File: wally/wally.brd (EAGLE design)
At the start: 41 x 101 mm, 94 parts, among them IC1 ESP32-S3-WROOM-1U-N16, IC2 XTLV61048DBVR, IC3 TLV1117LV33DCYR, IC4 DPS310XTSA1, IC5 BMI323, IC6 MCP96L00T-E_MX, IC7 MLX90395KLW-BBA-001-SP, J1 MSD-4-A, J2 QWIIC_RIGHT_ANGLE, J3 QWIIC_RIGHT_ANGLE, J4 S2B-PH-K-S(LF)(SN), J6 USBC, U1 RA-01H

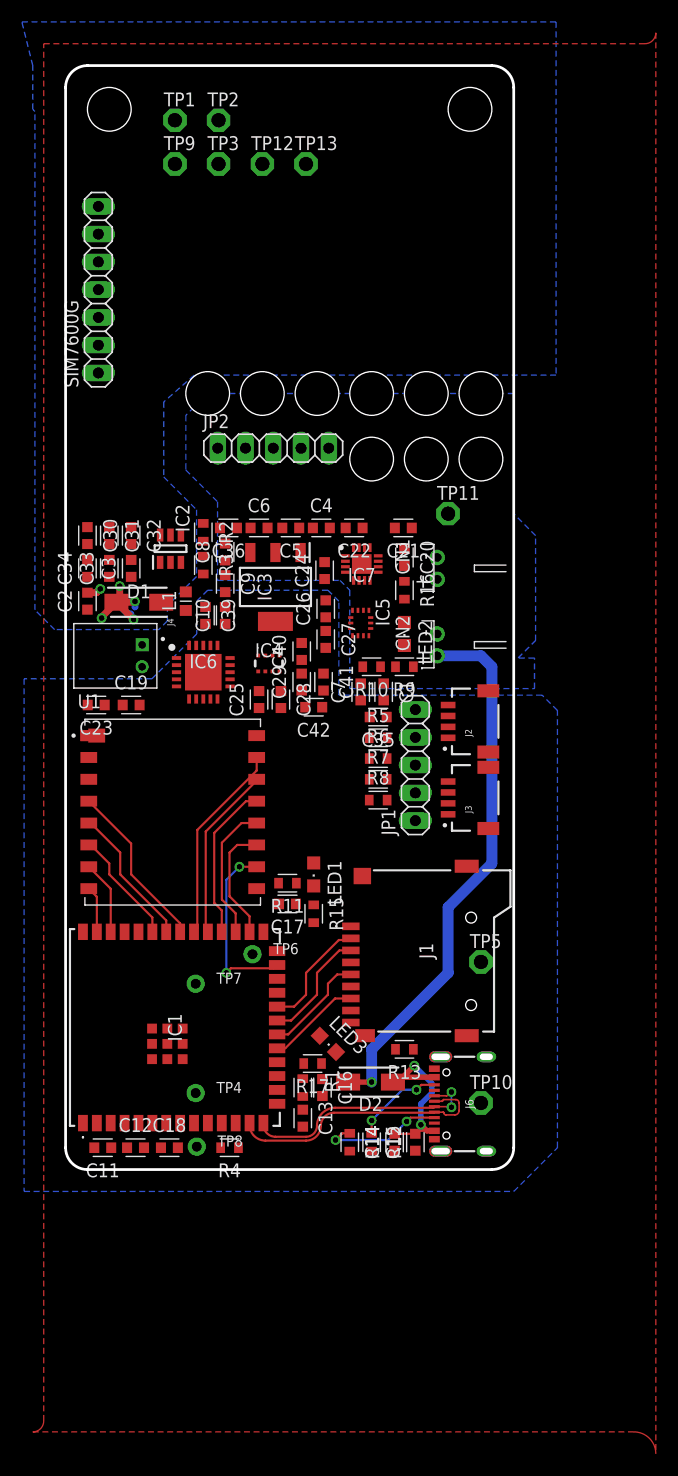
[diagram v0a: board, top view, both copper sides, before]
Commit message: high current traces
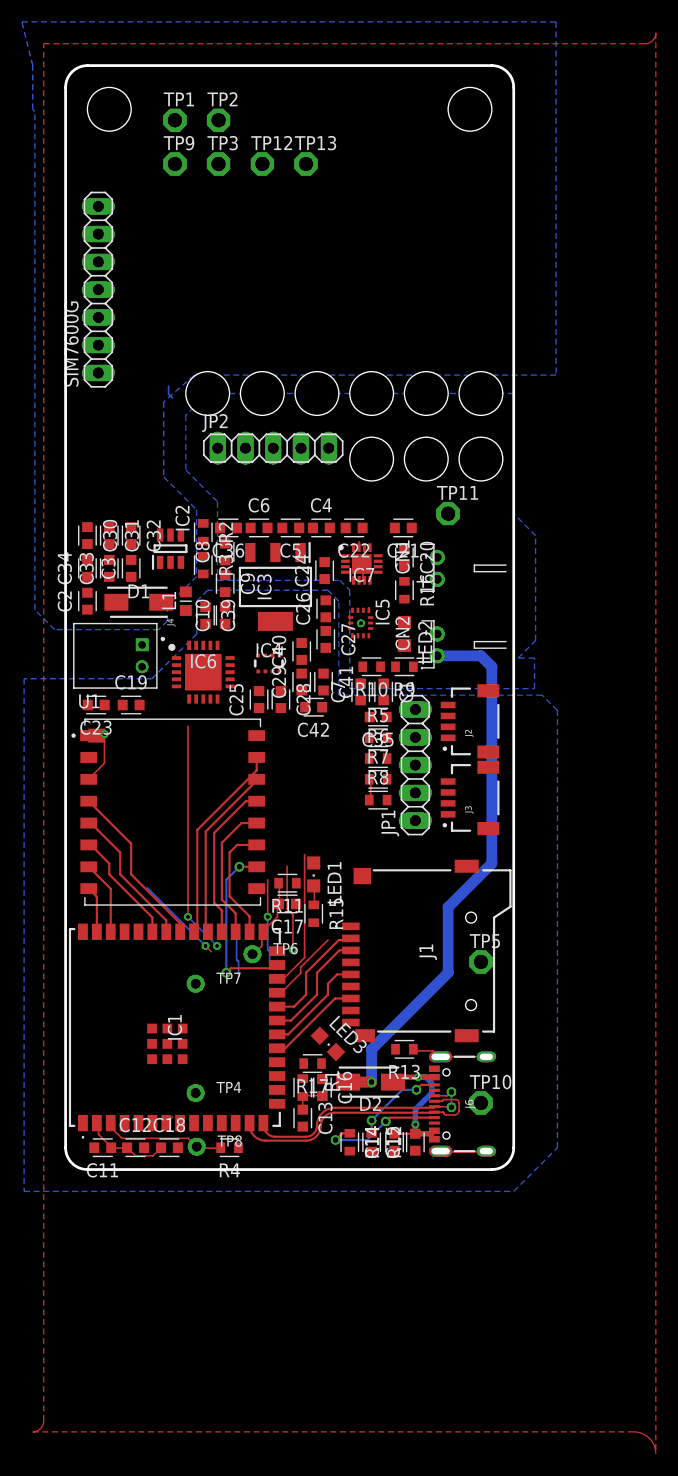
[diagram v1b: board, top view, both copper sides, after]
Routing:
- net RX1: track 0.00 -> 21.5 mm, vias 0 -> 2
- net 3V3: track 0.00 -> 18.3 mm, vias 0 -> 1
- net EN: track 0.00 -> 14.6 mm
- net SDA0: track 0.96 -> 14.0 mm
- net N$21: track 0.00 -> 11.3 mm
- net VSIM: track 10.9 -> 0.00 mm, vias 5 -> 0
- net SCL1: track 0.00 -> 9.54 mm, vias 0 -> 1
- net VSENSE: track 0.00 -> 9.32 mm, vias 0 -> 1
- net PPS: track 0.00 -> 8.41 mm, vias 0 -> 1
- net SCL0: track 0.00 -> 7.85 mm, vias 0 -> 1
- net BOOT: track 0.00 -> 7.64 mm
- net SDA1: track 0.00 -> 5.20 mm
- net VBUS: track 17.9 -> 15.8 mm
- net N$1: track 0.00 -> 1.76 mm
- net GND: track 0.00 -> 1.73 mm
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
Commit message: apply jlc drc
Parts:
- moved JP2 6.38 mm to (24.0, -31.0)
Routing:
- net VCC: track 51.6 -> 49.4 mm
- net TX1: track 1.44 -> 0.23 mm

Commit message: spider vsim
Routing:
- net VSIM: track 0.00 -> 21.4 mm, vias 0 -> 7
- net RX1: track 21.5 -> 0.30 mm, vias 2 -> 0
- net PPS: track 8.41 -> 0.11 mm, vias 1 -> 0
- net VSENSE: track 9.32 -> 1.60 mm, vias 1 -> 0
- net 3V3: track 18.3 -> 13.6 mm, vias 1 -> 0
- net SDA1: track 5.20 -> 0.68 mm
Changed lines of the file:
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@@
 <wire x1="27.9146" y1="-65.2526" x2="27.7848" y2="-65.3" width="0.1524" layer="1"/>
 <wire x1="27.9146" y1="-63.4746" x2="27.7848" y2="-63.4" width="0.1524" layer="1"/>
-<wire x1="3.556" y1="-63.8302" x2="3.556" y2="-61.1632" width="0.1524" layer="1"/>
-<wire x1="2.1336" y1="-65.2526" x2="3.556" y2="-63.8302" width="0.1524" layer="1"/>
 <wire x1="2.1336" y1="-65.2526" x2="2.1179" y2="-65.3" width="0.1524" layer="1"/>
 <wire x1="5.5118" y1="-99.0346" x2="4.2672" y2="-99.0346" width="0.1524" layer="1"/>
@@
 <wire x1="2.8448" y1="-96.7232" x2="2.86" y2="-96.75" width="0.1524" layer="1"/>
 <wire x1="29.5148" y1="-59.563" x2="29.3746" y2="-59.6" width="0.1524" layer="1"/>
-<via x="3.556" y="-61.1632" extent="1-16" drill="0.35"/>
 <wire x1="21.7" y1="-92.6848" x2="8.7254" y2="-99" width="0" layer="19" extent="1-1"/>
 <wire x1="25.9588" y1="-82.1436" x2="21.8694" y2="-92.6338" width="0" layer="19" extent="1-1"/>
@@
 <wire x1="27.9146" y1="-63.2968" x2="27.9146" y2="-61.5188" width="0" layer="19" extent="1-1"/>
 <wire x1="27.9146" y1="-65.2526" x2="27.9146" y2="-63.4746" width="0" layer="19" extent="1-1"/>
-<wire x1="3.5746" y1="-58.5" x2="3.556" y2="-61.1632" width="0" layer="19" extent="1-1"/>
-<wire x1="5.2254" y1="-58.5" x2="3.5746" y2="-58.5" width="0" layer="19" extent="1-1"/>
 <wire x1="34.4932" y1="-60.6298" x2="32" y2="-58.92" width="0" layer="19" extent="1-1"/>
 <wire x1="23.6" y1="-57.1746" x2="27.7368" y2="-61.341" width="0" layer="19" extent="1-1"/>
@@
 <wire x1="12.6" y1="-57.95" x2="17.7" y2="-57.2254" width="0" layer="19" extent="1-1"/>
 <wire x1="34.8488" y1="-67.3862" x2="34.4932" y2="-60.6298" width="0" layer="19" extent="1-1"/>
+<wire x1="5.2254" y1="-58.5" x2="12.6" y2="-57.95" width="0" layer="19" extent="1-1"/>
+<wire x1="3.5746" y1="-58.5" x2="5.2254" y2="-58.5" width="0" layer="19" extent="1-1"/>
+<wire x1="2.1336" y1="-65.2526" x2="3.5746" y2="-58.5" width="0" layer="19" extent="1-1"/>
 <wire x1="18" y1="-9" x2="19.2" y2="-44.55" width="0" layer="19" extent="1-1"/>
 </signal>
@@
 <vertex x="-3" y="0"/>
 </polygon>
-<wire x1="2" y1="-48.2254" x2="4.65" y2="-49.1" width="0" layer="19" extent="1-1"/>
-<wire x1="2" y1="-45.2254" x2="2" y2="-48.2254" width="0" layer="19" extent="1-1"/>
-<wire x1="2" y1="-43.7746" x2="2" y2="-45.2254" width="0" layer="19" extent="1-1"/>
-<wire x1="4" y1="-43.7746" x2="2" y2="-43.7746" width="0" layer="19" extent="1-1"/>
+<wire x1="2" y1="-43.7746" x2="6" y2="-43.7746" width="0.2" layer="1"/>
+<wire x1="2" y1="-45.2254" x2="4" y2="-45.2254" width="0.2" layer="1"/>
+<wire x1="2" y1="-45.2254" x2="2" y2="-43.7746" width="0.2" layer="1"/>
+<wire x1="2" y1="-48.2254" x2="2.8966" y2="-49.122" width="0.2" layer="1"/>
+<wire x1="2.8966" y1="-49.122" x2="3.175" y2="-49.122" width="0.2" layer="1"/>
+<wire x1="4.327" y1="-49.1" x2="3.144" y2="-47.917" width="0.5" layer="1"/>
+<wire x1="3.144" y1="-47.891" x2="3.144" y2="-47.917" width="0.2" layer="1"/>
+<wire x1="4.65" y1="-49.1" x2="4.327" y2="-49.1" width="0.2" layer="1"/>
+<via x="3.144" y="-47.891" extent="1-16" drill="0.35"/>
+<wire x1="4.65" y1="-49.1" x2="4.728" y2="-49.022" width="0.2" layer="1"/>
+<wire x1="4.728" y1="-49.022" x2="6.223" y2="-49.022" width="0.5" layer="1"/>
+<via x="6.223" y="-49.022" extent="1-16" drill="0.35"/>
+<wire x1="6.014" y1="-50.152" x2="4.962" y2="-49.1" width="0.5" layer="1"/>
+<wire x1="4.65" y1="-49.1" x2="4.962" y2="-49.1" width="0.2" layer="1"/>
+<wire x1="6.123" y1="-50.152" x2="6.161" y2="-50.114" width="0.2" layer="1"/>
+<wire x1="6.123" y1="-50.152" x2="6.014" y2="-50.152" width="0.2" layer="1"/>
+<via x="6.161" y="-50.114" extent="1-16" drill="0.35"/>
+<wire x1="4.65" y1="-49.1" x2="4.99" y2="-49.1" width="0.2" layer="1"/>
+<wire x1="6.161" y1="-47.891" x2="6.161" y2="-47.929" width="0.2" layer="1"/>
+<wire x1="6.161" y1="-47.929" x2="4.99" y2="-49.1" width="0.5" layer="1"/>
+<via x="6.161" y="-47.891" extent="1-16" drill="0.35"/>
+<wire x1="4.65" y1="-49.1" x2="4.65" y2="-50.191" width="0.5" layer="1"/>
+<wire x1="4.65" y1="-50.191" x2="4.716" y2="-50.257" width="0.2" layer="1"/>
+<via x="4.716" y="-50.257" extent="1-16" drill="0.35"/>
+<wire x1="4.65" y1="-49.1" x2="4.498" y2="-49.1" width="0.2" layer="1"/>
+<wire x1="4.498" y1="-49.1" x2="3.2505" y2="-50.3475" width="0.5" layer="1"/>
+<wire x1="3.2505" y1="-50.3475" x2="3.144" y2="-50.241" width="0.2" layer="1"/>
+<via x="3.144" y="-50.241" extent="1-16" drill="0.35"/>
+<wire x1="4.65" y1="-49.1" x2="4.628" y2="-49.122" width="0.2" layer="1"/>
+<wire x1="4.628" y1="-49.122" x2="3.175" y2="-49.122" width="0.5" layer="1"/>
+<via x="3.175" y="-49.122" extent="1-16" drill="0.35"/>
 <wire x1="4" y1="-45.2254" x2="4" y2="-43.7746" width="0" layer="19" extent="1-1"/>
-<wire x1="6" y1="-43.7746" x2="4" y2="-43.7746" width="0" layer="19" extent="1-1"/>
+<wire x1="3.144" y1="-47.891" x2="4" y2="-45.2254" width="0" layer="19" extent="1-1"/>
 <wire x1="12.6" y1="-41.8848" x2="6" y2="-43.7746" width="0" layer="19" extent="1-1"/>
 <wire x1="14.1254" y1="-42.3" x2="12.6" y2="-41.8848" width="0" layer="19" extent="1-1"/>
-<wire x1="3" y1="-17.96" x2="12.6" y2="-41.8848" width="0" layer="19" extent="1-1"/>
 </signal>
 <signal name="SLEEP">
@@
 <wire x1="34.8488" y1="-66.675" x2="35" y2="-66.5" width="0.1524" layer="1"/>
 <wire x1="6.7564" y1="-96.3676" x2="6.7564" y2="-96.7232" width="0.1524" layer="1"/>
-<wire x1="15.8242" y1="-81.9658" x2="15.8242" y2="-83.3882" width="0.1524" layer="16"/>
-<wire x1="15.6464" y1="-81.788" x2="15.8242" y2="-81.9658" width="0.1524" layer="16"/>
-<wire x1="15.6464" y1="-78.9432" x2="15.6464" y2="-81.788" width="0.1524" layer="16"/>
 <wire x1="6.7564" y1="-96.7232" x2="6.67" y2="-96.75" width="0.1524" layer="1"/>
-<wire x1="15.8242" y1="-83.3882" x2="6.7564" y2="-96.3676" width="0" layer="19" extent="1-16"/>
-<wire x1="29.4152" y1="-65.3" x2="15.6464" y2="-78.9432" width="0" layer="19" extent="1-16"/>
+<wire x1="29.4152" y1="-65.3" x2="6.7564" y2="-96.3676" width="0" layer="19" extent="1-1"/>
 <wire x1="34.8488" y1="-66.675" x2="29.4152" y2="-65.3" width="0" layer="19" extent="1-1"/>
 </signal>
@@
 <wire x1="30.0482" y1="-54.9402" x2="30.1848" y2="-55" width="0.1524" layer="1"/>
 <wire x1="28.448" y1="-55.118" x2="28.8036" y2="-55.118" width="0.1524" layer="1"/>
-<wire x1="18.4912" y1="-77.8764" x2="18.4912" y2="-74.4982" width="0.1524" layer="1"/>
-<wire x1="18.4912" y1="-80.899" x2="18.4912" y2="-77.8764" width="0.1524" layer="16"/>
-<wire x1="18.669" y1="-81.0768" x2="18.4912" y2="-80.899" width="0.1524" layer="16"/>
-<wire x1="18.669" y1="-82.1436" x2="18.669" y2="-81.0768" width="0.1524" layer="16"/>
 <wire x1="9.2456" y1="-96.7232" x2="9.779" y2="-96.1898" width="0.1524" layer="1"/>
 <wire x1="28.8036" y1="-55.118" x2="28.8152" y2="-55" width="0.1524" layer="1"/>
 <wire x1="9.2456" y1="-96.7232" x2="9.21" y2="-96.75" width="0.1524" layer="1"/>
-<via x="18.4912" y="-77.8764" extent="1-16" drill="0.35"/>
-<wire x1="18.669" y1="-82.1436" x2="9.779" y2="-96.1898" width="0" layer="19" extent="1-16"/>
-<wire x1="28.448" y1="-55.118" x2="18.4912" y2="-74.4982" width="0" layer="19" extent="1-1"/>
+<wire x1="28.448" y1="-55.118" x2="9.779" y2="-96.1898" width="0" layer="19" extent="1-1"/>
 <wire x1="30.0482" y1="-54.9402" x2="28.9814" y2="-54.9402" width="0" layer="19" extent="1-1"/>
 </signal>
@@
 <contactref element="JP2" pad="3"/>
 <contactref element="IC1" pad="10"/>
-<wire x1="11.2014" y1="-77.8764" x2="13.8684" y2="-80.5434" width="0.1524" layer="16"/>
-<wire x1="11.2014" y1="-60.452" x2="11.2014" y2="-77.8764" width="0.1524" layer="1"/>
 <wire x1="13.1572" y1="-96.7232" x2="13.02" y2="-96.75" width="0.1524" layer="1"/>
 <wire x1="2.8448" y1="-25.6032" x2="3" y2="-25.58" width="0.1524" layer="1"/>
-<via x="13.8684" y="-80.5434" extent="1-16" drill="0.35"/>
-<via x="11.2014" y="-77.8764" extent="1-16" drill="0.35"/>
-<wire x1="13.8684" y1="-80.5434" x2="13.1572" y2="-96.7232" width="0" layer="19" extent="1-1"/>
-<wire x1="24" y1="-31.03" x2="11.2014" y2="-60.452" width="0" layer="19" extent="1-1"/>
+<wire x1="24" y1="-31.03" x2="13.1572" y2="-96.7232" width="0" layer="19" extent="1-1"/>
 <wire x1="3" y1="-25.58" x2="24" y2="-31.03" width="0" layer="19" extent="1-1"/>
 </signal>
@@
 <contactref element="JP2" pad="5"/>
 <contactref element="IC1" pad="8"/>
-<wire x1="12.8016" y1="-80.5434" x2="13.335" y2="-81.0768" width="0.1524" layer="1"/>
-<wire x1="7.4676" y1="-75.2094" x2="12.8016" y2="-80.5434" width="0.1524" layer="16"/>
 <wire x1="10.4902" y1="-96.7232" x2="10.48" y2="-96.75" width="0.1524" layer="1"/>
 <wire x1="29.003" y1="-31.0566" x2="29.08" y2="-31.03" width="0.1524" layer="16"/>
-<via x="12.8016" y="-80.5434" extent="1-16" drill="0.35"/>
-<wire x1="13.335" y1="-81.0768" x2="10.4902" y2="-96.7232" width="0" layer="19" extent="1-1"/>
-<wire x1="29.003" y1="-31.0566" x2="7.4676" y2="-75.2094" width="0" layer="19" extent="16-16"/>
+<wire x1="29.003" y1="-31.0566" x2="10.4902" y2="-96.7232" width="0" layer="19" extent="1-16"/>
 </signal>
 </signals>

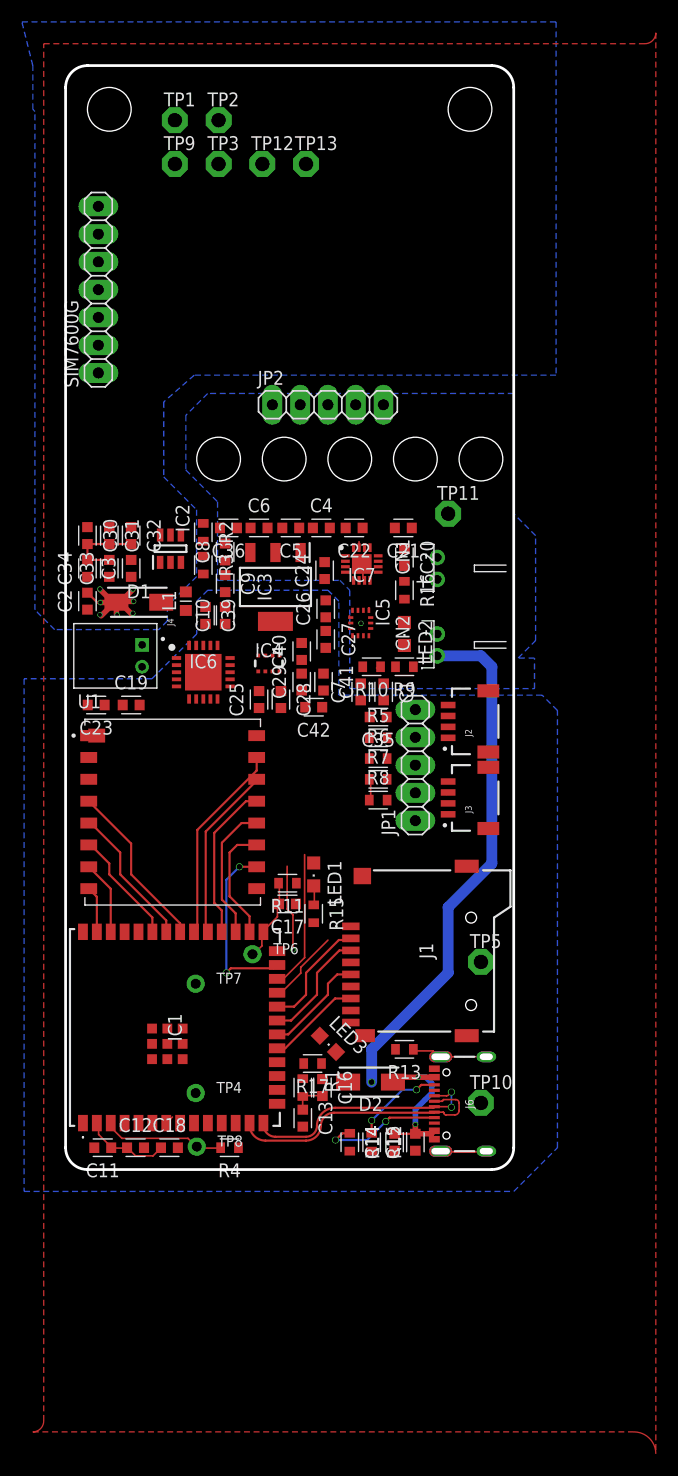
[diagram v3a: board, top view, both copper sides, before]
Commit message: remove autotrace attempt
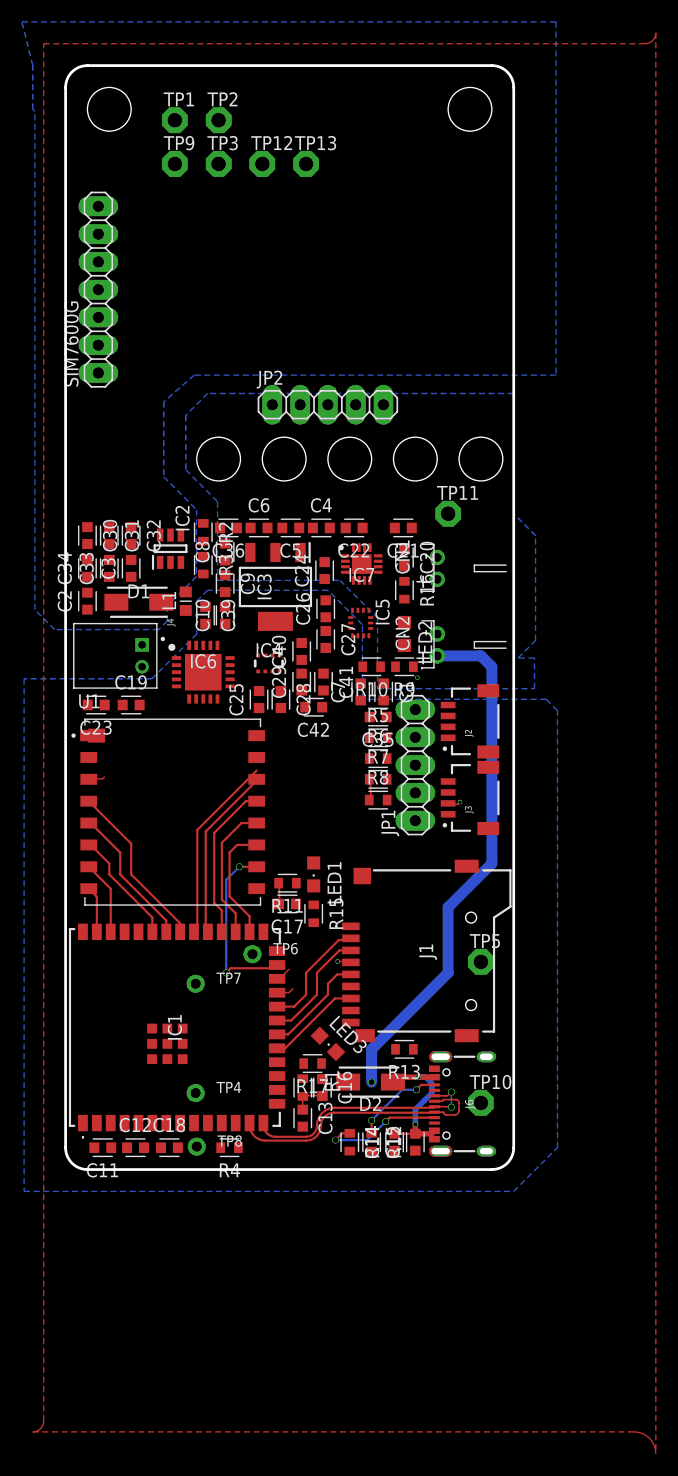
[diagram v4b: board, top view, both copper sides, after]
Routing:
- net VSIM: track 21.4 -> 0.00 mm, vias 7 -> 0
- net N$21: track 11.3 -> 0.68 mm
- net EN: track 14.6 -> 4.08 mm
- net SDA0: track 14.0 -> 3.85 mm
- net SCL1: track 9.54 -> 1.90 mm, vias 1 -> 0
- net BOOT: track 7.64 -> 2.56 mm
- net 3V3: track 13.6 -> 9.28 mm, vias 0 -> 2
- net SCL0: track 7.85 -> 5.57 mm
- net SLEEP: track 1.33 -> 3.16 mm
- net GND: track 1.73 -> 0.13 mm
- net VSENSE: track 1.60 -> 0.04 mm
- net TX1: track 0.23 -> 1.69 mm
- net N$1: track 1.76 -> 0.33 mm
- net RAD_CS: track 18.3 -> 17.1 mm
- net SDA1: track 0.68 -> 1.73 mm
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
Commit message: autoroute with thicker traces
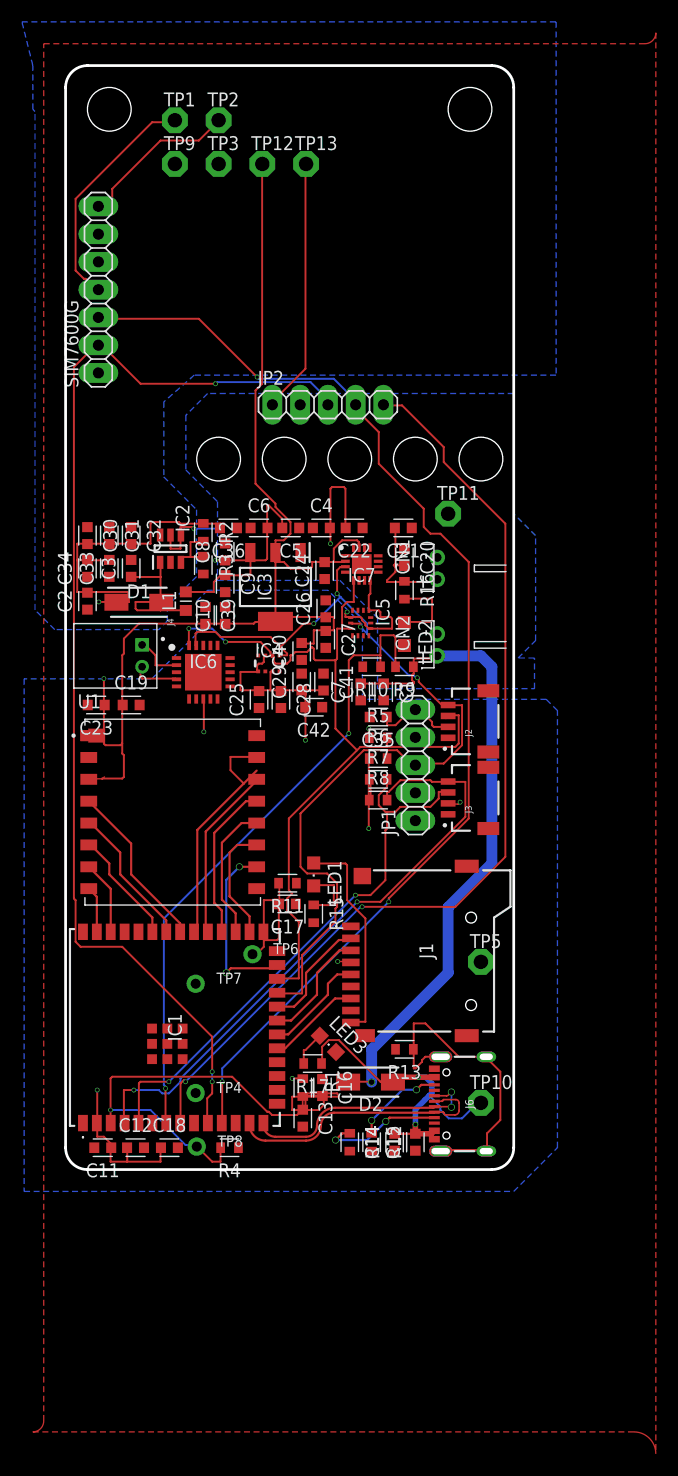
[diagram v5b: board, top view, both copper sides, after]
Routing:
- net 3V3: track 9.28 -> 181.8 mm, vias 2 -> 10
- net TX1: track 1.69 -> 108.7 mm, vias 0 -> 3
- net RX1: track 0.19 -> 103.9 mm, vias 0 -> 3
- net PPS: track 0.03 -> 89.1 mm, vias 0 -> 2
- net VCC: track 49.0 -> 135.7 mm, vias 1 -> 4
- net SCL0: track 5.57 -> 89.8 mm, vias 1 -> 4
- net SDA0: track 3.85 -> 80.4 mm, vias 0 -> 2
- net VSENSE: track 0.04 -> 59.6 mm, vias 0 -> 2
- net SCL1: track 1.90 -> 58.6 mm, vias 0 -> 2
- net SDA1: track 1.73 -> 52.6 mm, vias 0 -> 2
- net EN: track 4.08 -> 54.0 mm, vias 0 -> 1
- net VSIM: track 0.00 -> 31.3 mm, vias 0 -> 1
- net N$21: track 0.68 -> 29.4 mm
- net PWRKEY: track 0.52 -> 22.4 mm
- net N$49: track 2.12 -> 21.1 mm
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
